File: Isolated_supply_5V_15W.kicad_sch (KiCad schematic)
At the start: 19 parts, among them U15 LM5576

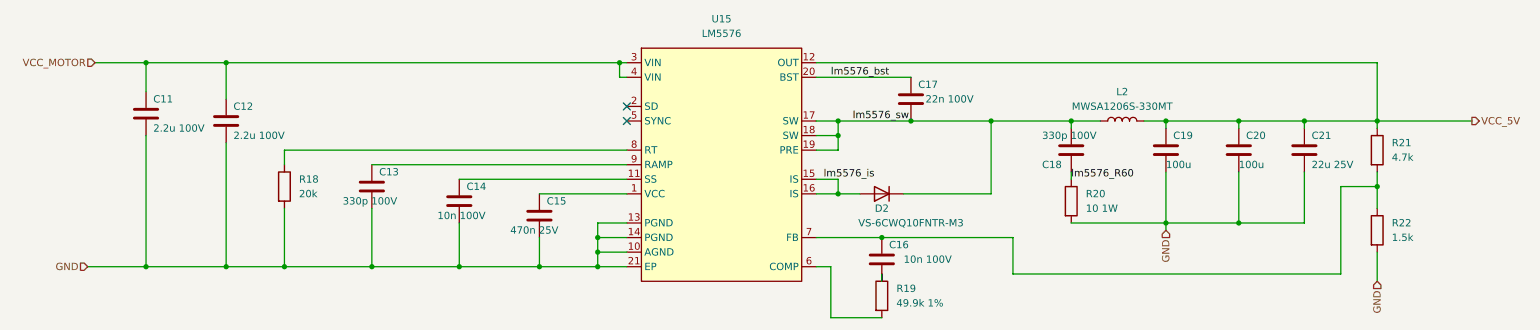
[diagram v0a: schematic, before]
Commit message: Refactored top sheet
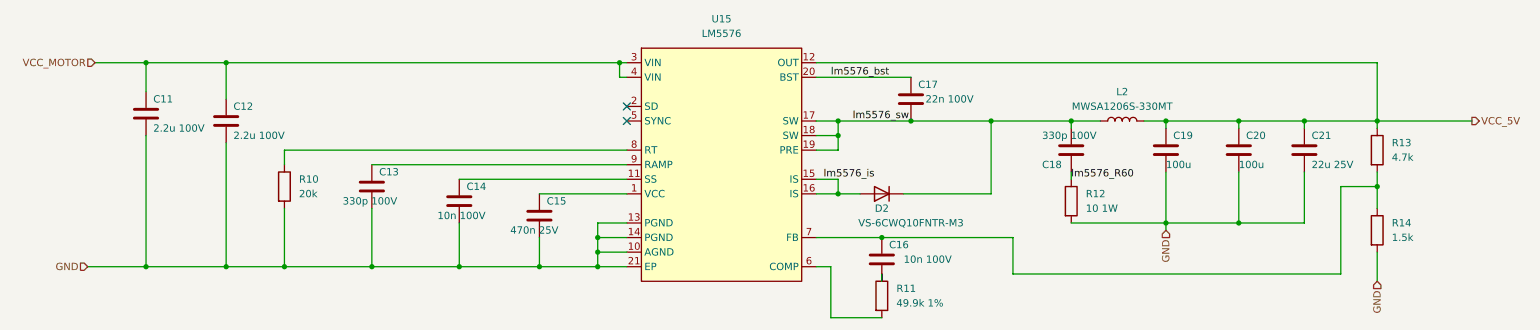
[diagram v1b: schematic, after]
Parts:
- renumbered R18 to R10, R19 to R11, R20 to R12, R21 to R13, R22 to R14
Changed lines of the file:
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@@
   (symbol (lib_id "Device:R") (at 254 97.79 0) (unit 1)
     (in_bom yes) (on_board yes) (fields_autoplaced)
-    (property "Reference" "R22" (id 0) (at 256.54 96.5199 0)
+    (property "Reference" "R14" (id 0) (at 256.54 96.5199 0)
       (effects (font (size 1.27 1.27)) (justify left))
     )
@@
   (symbol (lib_id "Device:R") (at 200.66 92.71 0) (unit 1)
     (in_bom yes) (on_board yes) (fields_autoplaced)
-    (property "Reference" "R20" (id 0) (at 203.2 91.4399 0)
+    (property "Reference" "R12" (id 0) (at 203.2 91.4399 0)
       (effects (font (size 1.27 1.27)) (justify left))
     )
@@
   (symbol (lib_id "Device:R") (at 63.5 90.17 0) (unit 1)
     (in_bom yes) (on_board yes) (fields_autoplaced)
-    (property "Reference" "R18" (id 0) (at 66.04 88.8999 0)
+    (property "Reference" "R10" (id 0) (at 66.04 88.8999 0)
       (effects (font (size 1.27 1.27)) (justify left))
     )
@@
   (symbol (lib_id "Device:R") (at 167.64 109.22 0) (unit 1)
     (in_bom yes) (on_board yes)
-    (property "Reference" "R19" (id 0) (at 170.18 107.9499 0)
+    (property "Reference" "R11" (id 0) (at 170.18 107.9499 0)
       (effects (font (size 1.27 1.27)) (justify left))
     )
@@
   (symbol (lib_id "Device:R") (at 254 83.82 0) (unit 1)
     (in_bom yes) (on_board yes) (fields_autoplaced)
-    (property "Reference" "R21" (id 0) (at 256.54 82.5499 0)
+    (property "Reference" "R13" (id 0) (at 256.54 82.5499 0)
       (effects (font (size 1.27 1.27)) (justify left))
     )
